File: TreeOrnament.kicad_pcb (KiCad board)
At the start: 2 copper layers, 80 x 99 mm, 44 parts, among them J1 USB_B_Micro

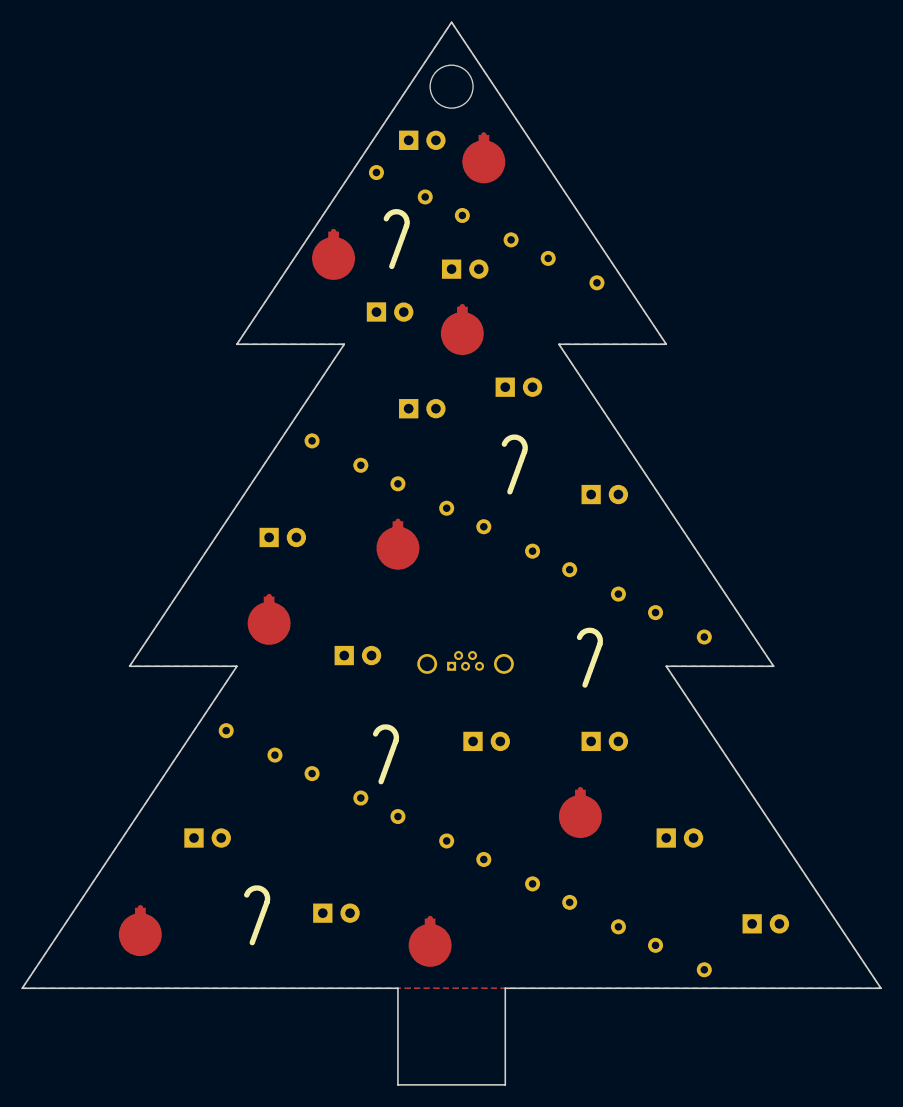
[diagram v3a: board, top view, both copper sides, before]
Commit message: wire LEDs to resistors
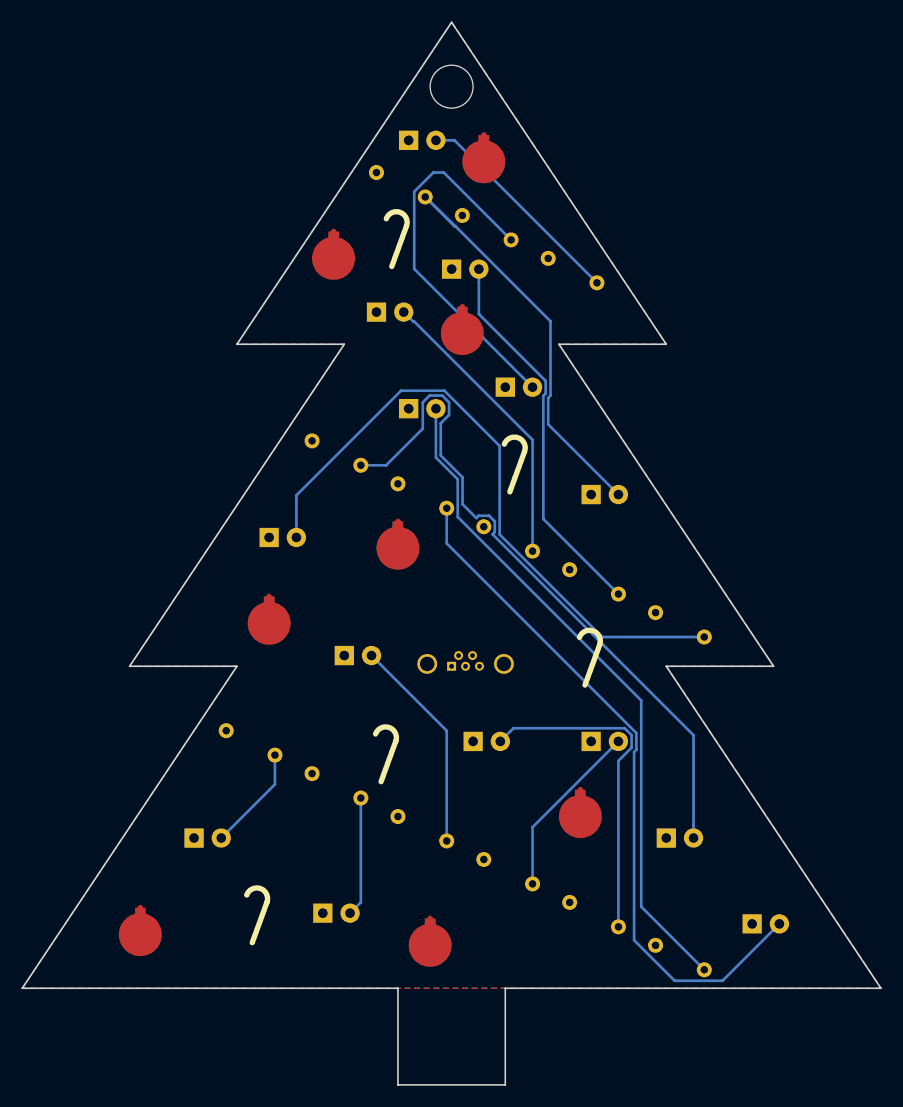
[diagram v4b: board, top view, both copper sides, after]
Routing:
- net Net-(D8-Pad2): track 0.00 -> 65.0 mm
- net Net-(D7-Pad2): track 0.00 -> 64.4 mm
- net Net-(D6-Pad2): track 0.00 -> 62.6 mm
- net Net-(D11-Pad2): track 0.00 -> 60.3 mm
- net Net-(D12-Pad2): track 0.00 -> 39.4 mm
- net Net-(D10-Pad2): track 0.00 -> 35.8 mm
- net Net-(D13-Pad2): track 0.00 -> 35.1 mm
- net Net-(D5-Pad2): track 0.00 -> 31.4 mm
- net Net-(D9-Pad2): track 0.00 -> 27.3 mm
- net Net-(D14-Pad2): track 0.00 -> 20.5 mm
- net Net-(D3-Pad2): track 0.00 -> 20.2 mm
- net Net-(D4-Pad2): track 0.00 -> 16.6 mm
- net Net-(D2-Pad2): track 0.00 -> 11.1 mm
- net Net-(D1-Pad2): track 0.00 -> 9.80 mm
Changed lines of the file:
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@@
     (thickness 1.6)
     (drawings 17)
-    (tracks 0)
+    (tracks 86)
     (zones 0)
     (modules 44)
@@
   (gr_line (start 115 60) (end 125 60) (angle 90) (layer Edge.Cuts) (width 0.15))
   (gr_line (start 135 30) (end 115 60) (angle 90) (layer Edge.Cuts) (width 0.15))
+  (segment (start 118.542304 98.274616) (end 118.542304 100.997696) (width 0.25) (layer B.Cu) (net 2))
+  (segment (start 118.542304 100.997696) (end 113.54 106) (width 0.25) (layer B.Cu) (net 2))
+  (segment (start 126.542304 102.274616) (end 126.542304 111.997696) (width 0.25) (layer B.Cu) (net 3))
+  (segment (start 126.542304 111.997696) (end 125.54 113) (width 0.25) (layer B.Cu) (net 3))
+  (segment (start 134.542304 106.274616) (end 134.542304 96.002304) (width 0.25) (layer B.Cu) (net 4))
+  (segment (start 134.542304 96.002304) (end 127.54 89) (width 0.25) (layer B.Cu) (net 4))
+  (segment (start 142.542304 110.274616) (end 142.542304 104.997696) (width 0.25) (layer B.Cu) (net 5))
+  (segment (start 142.542304 104.997696) (end 150.54 97) (width 0.25) (layer B.Cu) (net 5))
+  (segment (start 140.439999 96.100001) (end 139.54 97) (width 0.25) (layer B.Cu) (net 6))
+  (segment (start 151.128001 95.774999) (end 140.765001 95.774999) (width 0.25) (layer B.Cu) (net 6))
+  (segment (start 151.765001 96.411999) (end 151.128001 95.774999) (width 0.25) (layer B.Cu) (net 6))
+  (segment (start 150.542304 98.810698) (end 151.765001 97.588001) (width 0.25) (layer B.Cu) (net 6))
+  (segment (start 150.542304 114.274616) (end 150.542304 98.810698) (width 0.25) (layer B.Cu) (net 6))
+  (segment (start 140.765001 95.774999) (end 140.439999 96.100001) (width 0.25) (layer B.Cu) (net 6))
+  (segment (start 151.765001 97.588001) (end 151.765001 96.411999) (width 0.25) (layer B.Cu) (net 6))
+  (segment (start 135.567305 76.084307) (end 135.567305 72.582489) (width 0.25) (layer B.Cu) (net 7))
+  (segment (start 133.54 67.272792) (end 133.54 66) (width 0.25) (layer B.Cu) (net 7))
+  (segment (start 135.567305 72.582489) (end 133.54 70.555184) (width 0.25) (layer B.Cu) (net 7))
+  (segment (start 152.665023 112.397335) (end 152.665023 93.182025) (width 0.25) (layer B.Cu) (net 7))
+  (segment (start 158.542304 118.274616) (end 152.665023 112.397335) (width 0.25) (layer B.Cu) (net 7))
+  (segment (start 152.665023 93.182025) (end 135.567305 76.084307) (width 0.25) (layer B.Cu) (net 7))
+  (segment (start 133.54 70.555184) (end 133.54 67.272792) (width 0.25) (layer B.Cu) (net 7))
+  (segment (start 157.54 104.727208) (end 157.54 106) (width 0.25) (layer B.Cu) (net 8))
+  (segment (start 157.54 96.425725) (end 157.54 104.727208) (width 0.25) (layer B.Cu) (net 8))
+  (segment (start 138.815639 77.701363) (end 157.54 96.425725) (width 0.25) (layer B.Cu) (net 8))
+  (segment (start 128.902384 71.274616) (end 132.314999 67.862001) (width 0.25) (layer B.Cu) (net 8))
+  (segment (start 139.025001 76.507999) (end 139.025001 77.492001) (width 0.25) (layer B.Cu) (net 8))
+  (segment (start 132.314999 65.411999) (end 132.951999 64.774999) (width 0.25) (layer B.Cu) (net 8))
+  (segment (start 134.765001 65.411999) (end 134.765001 66.588001) (width 0.25) (layer B.Cu) (net 8))
+  (segment (start 137.507999 75.974999) (end 138.492001 75.974999) (width 0.25) (layer B.Cu) (net 8))
+  (segment (start 137.298636 76.184362) (end 137.507999 75.974999) (width 0.25) (layer B.Cu) (net 8))
+  (segment (start 136.017315 74.90304) (end 137.298636 76.184362) (width 0.25) (layer B.Cu) (net 8))
+  (segment (start 133.99001 67.362992) (end 133.99001 70.368784) (width 0.25) (layer B.Cu) (net 8))
+  (segment (start 136.017315 72.396089) (end 136.017315 74.90304) (width 0.25) (layer B.Cu) (net 8))
+  (segment (start 134.128001 64.774999) (end 134.765001 65.411999) (width 0.25) (layer B.Cu) (net 8))
+  (segment (start 134.765001 66.588001) (end 133.99001 67.362992) (width 0.25) (layer B.Cu) (net 8))
+  (segment (start 132.951999 64.774999) (end 134.128001 64.774999) (width 0.25) (layer B.Cu) (net 8))
+  (segment (start 126.542304 71.274616) (end 128.902384 71.274616) (width 0.25) (layer B.Cu) (net 8))
+  (segment (start 133.99001 70.368784) (end 136.017315 72.396089) (width 0.25) (layer B.Cu) (net 8))
+  (segment (start 132.314999 67.862001) (end 132.314999 65.411999) (width 0.25) (layer B.Cu) (net 8))
+  (segment (start 139.025001 77.492001) (end 138.815639 77.701363) (width 0.25) (layer B.Cu) (net 8))
+  (segment (start 138.492001 75.974999) (end 139.025001 76.507999) (width 0.25) (layer B.Cu) (net 8))
+  (segment (start 152 97.989413) (end 152 115.517002) (width 0.25) (layer B.Cu) (net 9))
+  (segment (start 152 115.517002) (end 155.782615 119.299617) (width 0.25) (layer B.Cu) (net 9))
+  (segment (start 155.782615 119.299617) (end 160.240383 119.299617) (width 0.25) (layer B.Cu) (net 9))
+  (segment (start 160.240383 119.299617) (end 164.640001 114.899999) (width 0.25) (layer B.Cu) (net 9))
+  (segment (start 164.640001 114.899999) (end 165.54 114) (width 0.25) (layer B.Cu) (net 9))
+  (segment (start 134.542304 75.274616) (end 134.542304 78.552891) (width 0.25) (layer B.Cu) (net 9))
+  (segment (start 134.542304 78.552891) (end 152.215012 96.225599) (width 0.25) (layer B.Cu) (net 9))
+  (segment (start 152.215012 96.225599) (end 152.215012 97.774401) (width 0.25) (layer B.Cu) (net 9))
+  (segment (start 152.215012 97.774401) (end 152 97.989413) (width 0.25) (layer B.Cu) (net 9))
+  (segment (start 137.54 57.186998) (end 137.54 54.272792) (width 0.25) (layer B.Cu) (net 14))
+  (segment (start 143.765001 63.411999) (end 137.54 57.186998) (width 0.25) (layer B.Cu) (net 14))
+  (segment (start 143.765001 64.588001) (end 143.765001 63.411999) (width 0.25) (layer B.Cu) (net 14))
+  (segment (start 143.549989 64.803013) (end 143.765001 64.588001) (width 0.25) (layer B.Cu) (net 14))
+  (segment (start 143.549989 76.282301) (end 143.549989 64.803013) (width 0.25) (layer B.Cu) (net 14))
+  (segment (start 150.542304 83.274616) (end 143.549989 76.282301) (width 0.25) (layer B.Cu) (net 14))
+  (segment (start 137.54 54.272792) (end 137.54 53) (width 0.25) (layer B.Cu) (net 14))
+  (segment (start 139.475012 69.475012) (end 134.324988 64.324988) (width 0.25) (layer B.Cu) (net 15))
+  (segment (start 134.324988 64.324988) (end 130.29001 64.324988) (width 0.25) (layer B.Cu) (net 15))
+  (segment (start 130.29001 64.324988) (end 120.54 74.074998) (width 0.25) (layer B.Cu) (net 15))
+  (segment (start 120.54 74.074998) (end 120.54 76.727208) (width 0.25) (layer B.Cu) (net 15))
+  (segment (start 120.54 76.727208) (end 120.54 78) (width 0.25) (layer B.Cu) (net 15))
+  (segment (start 158.542304 87.274616) (end 149.025302 87.274616) (width 0.25) (layer B.Cu) (net 15))
+  (segment (start 149.025302 87.274616) (end 139.475012 77.724325) (width 0.25) (layer B.Cu) (net 15))
+  (segment (start 139.475012 77.724325) (end 139.475012 69.475012) (width 0.25) (layer B.Cu) (net 15))
+  (segment (start 144 64.989413) (end 144 67.46) (width 0.25) (layer B.Cu) (net 16))
+  (segment (start 144 67.46) (end 150.54 74) (width 0.25) (layer B.Cu) (net 16))
+  (segment (start 132.542304 46.274616) (end 135.292689 49.025001) (width 0.25) (layer B.Cu) (net 16))
+  (segment (start 135.292689 49.025001) (end 135.378003 49.025001) (width 0.25) (layer B.Cu) (net 16))
+  (segment (start 135.378003 49.025001) (end 132.542304 46.274616) (width 0.25) (layer B.Cu) (net 16))
+  (segment (start 135.378003 49.025001) (end 144.215012 57.86201) (width 0.25) (layer B.Cu) (net 16))
+  (segment (start 144.215012 57.86201) (end 144.215012 64.774401) (width 0.25) (layer B.Cu) (net 16))
+  (segment (start 144.215012 64.774401) (end 144 64.989413) (width 0.25) (layer B.Cu) (net 16))
+  (segment (start 134.267688 44) (end 133.299918 44) (width 0.25) (layer B.Cu) (net 17))
+  (segment (start 133.299918 44) (end 131.517303 45.782615) (width 0.25) (layer B.Cu) (net 17))
+  (segment (start 131.517303 45.782615) (end 131.517303 52.977303) (width 0.25) (layer B.Cu) (net 17))
+  (segment (start 131.517303 52.977303) (end 141.640001 63.100001) (width 0.25) (layer B.Cu) (net 17))
+  (segment (start 141.640001 63.100001) (end 142.54 64) (width 0.25) (layer B.Cu) (net 17))
+  (segment (start 140.542304 50.274616) (end 134.267688 44) (width 0.25) (layer B.Cu) (net 17))
+  (segment (start 148.542304 54.274616) (end 135.267688 41) (width 0.25) (layer B.Cu) (net 18))
+  (segment (start 135.267688 41) (end 133.54 41) (width 0.25) (layer B.Cu) (net 18))
+  (segment (start 131.439999 57.899999) (end 130.54 57) (width 0.25) (layer B.Cu) (net 19))
+  (segment (start 142.542304 79.274616) (end 142.542304 68.905893) (width 0.25) (layer B.Cu) (net 19))
+  (segment (start 131.53641 57.899999) (end 131.439999 57.899999) (width 0.25) (layer B.Cu) (net 19))
+  (segment (start 142.542304 68.905893) (end 131.53641 57.899999) (width 0.25) (layer B.Cu) (net 19))
   (zone (net 1) (net_name GND) (layer F.Cu) (hatch edge 0.508)
     (connect_pads (clearance 0.508))

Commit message: finish wiring up the tree
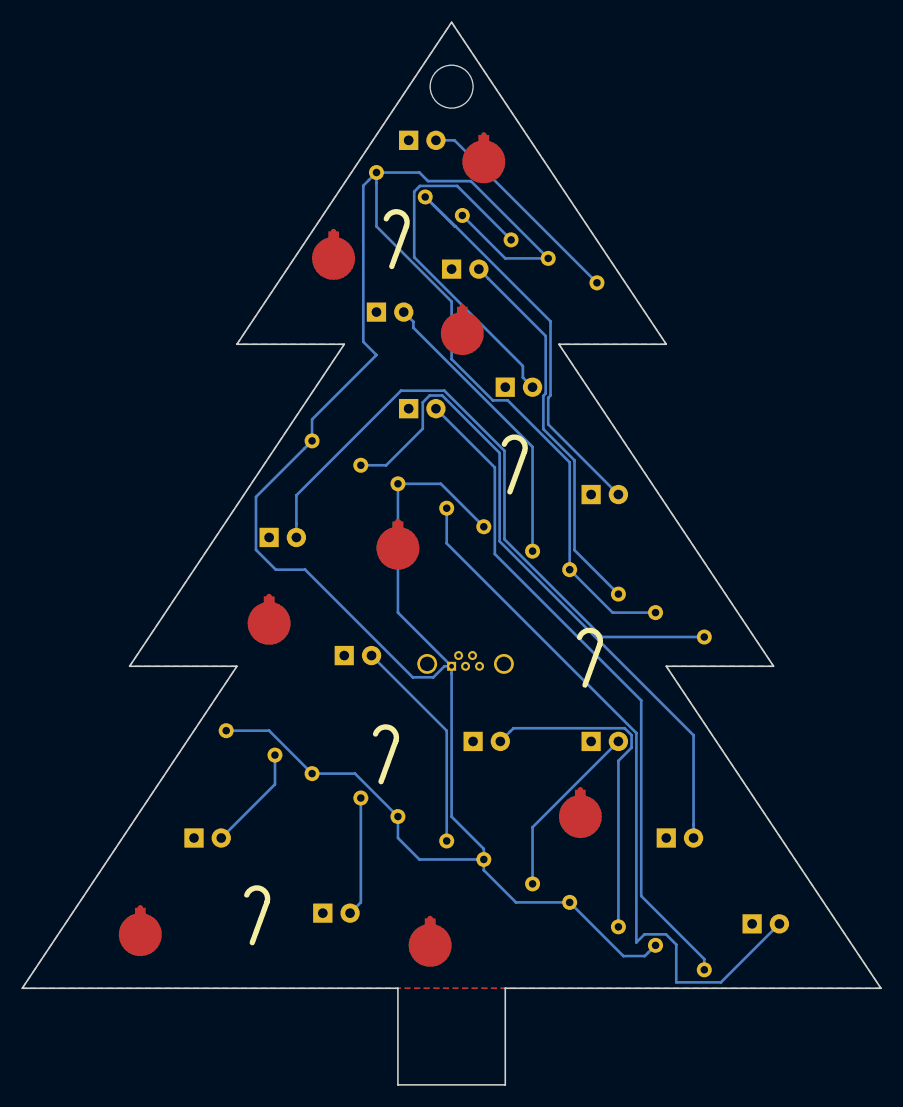
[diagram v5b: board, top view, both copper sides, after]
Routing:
- net +5V: track 0.00 -> 247.1 mm
- net Net-(D8-Pad2): track 65.0 -> 67.6 mm
- net Net-(D7-Pad2): track 64.4 -> 62.6 mm
- net Net-(D13-Pad2): track 35.1 -> 34.1 mm

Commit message: Propagate 150 Ohms to PCB, not that it really matters.
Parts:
- R1, R10, R11, R12, R13, R14, R2, R3, R4, R5, R6, R7, R8, R9: value 56 -> 150
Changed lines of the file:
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@@
       (effects (font (size 1 1) (thickness 0.15)))
     )
-    (fp_text value 56 (at 2.54 1.86 333.4) (layer F.Fab) hide
+    (fp_text value 150 (at 2.54 1.86 333.4) (layer F.Fab) hide
       (effects (font (size 1 1) (thickness 0.15)))
     )
@@
       (effects (font (size 1 1) (thickness 0.15)))
     )
-    (fp_text value 56 (at 2.54 1.86 333.4) (layer F.Fab) hide
+    (fp_text value 150 (at 2.54 1.86 333.4) (layer F.Fab) hide
       (effects (font (size 1 1) (thickness 0.15)))
     )
@@
       (effects (font (size 1 1) (thickness 0.15)))
     )
-    (fp_text value 56 (at 2.54 1.86 333.4) (layer F.Fab) hide
+    (fp_text value 150 (at 2.54 1.86 333.4) (layer F.Fab) hide
       (effects (font (size 1 1) (thickness 0.15)))
     )
@@
       (effects (font (size 1 1) (thickness 0.15)))
     )
-    (fp_text value 56 (at 2.54 1.86 333.4) (layer F.Fab) hide
+    (fp_text value 150 (at 2.54 1.86 333.4) (layer F.Fab) hide
       (effects (font (size 1 1) (thickness 0.15)))
     )
@@
       (effects (font (size 1 1) (thickness 0.15)))
     )
-    (fp_text value 56 (at 2.54 1.86 333.4) (layer F.Fab) hide
+    (fp_text value 150 (at 2.54 1.86 333.4) (layer F.Fab) hide
       (effects (font (size 1 1) (thickness 0.15)))
     )
@@
       (effects (font (size 1 1) (thickness 0.15)))
     )
-    (fp_text value 56 (at 2.54 1.86 333.4) (layer F.Fab) hide
+    (fp_text value 150 (at 2.54 1.86 333.4) (layer F.Fab) hide
       (effects (font (size 1 1) (thickness 0.15)))
     )
@@
       (effects (font (size 1 1) (thickness 0.15)))
     )
-    (fp_text value 56 (at 2.54 1.86 333.4) (layer F.Fab) hide
+    (fp_text value 150 (at 2.54 1.86 333.4) (layer F.Fab) hide
       (effects (font (size 1 1) (thickness 0.15)))
     )
@@
       (effects (font (size 1 1) (thickness 0.15)))
     )
-    (fp_text value 56 (at 2.54 1.86 333.4) (layer F.Fab) hide
+    (fp_text value 150 (at 2.54 1.86 333.4) (layer F.Fab) hide
       (effects (font (size 1 1) (thickness 0.15)))
     )
@@
       (effects (font (size 1 1) (thickness 0.15)))
     )
-    (fp_text value 56 (at 2.54 1.86 333.4) (layer F.Fab) hide
+    (fp_text value 150 (at 2.54 1.86 333.4) (layer F.Fab) hide
       (effects (font (size 1 1) (thickness 0.15)))
     )
@@
       (effects (font (size 1 1) (thickness 0.15)))
     )
-    (fp_text value 56 (at 2.54 1.86 333.4) (layer F.Fab) hide
+    (fp_text value 150 (at 2.54 1.86 333.4) (layer F.Fab) hide
       (effects (font (size 1 1) (thickness 0.15)))
     )
@@
       (effects (font (size 1 1) (thickness 0.15)))
     )
-    (fp_text value 56 (at 2.54 1.86 333.4) (layer F.Fab) hide
+    (fp_text value 150 (at 2.54 1.86 333.4) (layer F.Fab) hide
       (effects (font (size 1 1) (thickness 0.15)))
     )
@@
       (effects (font (size 1 1) (thickness 0.15)))
     )
-    (fp_text value 56 (at 2.54 1.86 333.4) (layer F.Fab) hide
+    (fp_text value 150 (at 2.54 1.86 333.4) (layer F.Fab) hide
       (effects (font (size 1 1) (thickness 0.15)))
     )
@@
       (effects (font (size 1 1) (thickness 0.15)))
     )
-    (fp_text value 56 (at 2.54 1.86 333.4) (layer F.Fab) hide
+    (fp_text value 150 (at 2.54 1.86 333.4) (layer F.Fab) hide
       (effects (font (size 1 1) (thickness 0.15)))
     )
@@
       (effects (font (size 1 1) (thickness 0.15)))
     )
-    (fp_text value 56 (at 2.54 1.86 333.4) (layer F.Fab) hide
-      (effects (font (size 1 1) (thickness 0.15)))
-    )
+    (fp_text value 150 (at 2.54 1.86 333.4) (layer F.Fab) hide
+      (effects (font (size 1 1) (thickness 0.15)))
+    )
